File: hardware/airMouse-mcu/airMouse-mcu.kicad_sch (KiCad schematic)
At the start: 51 parts, among them J4 AT, J5 RADIO_PRG, J6 MCU_PRG, Q1 IRLML6346, SW60 KEY, U1 STM32G071RBTx, U2 AP1603, U3 ESP32-C3-WROOM-02U, U4 LSM6DS3

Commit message: add mouse pcb
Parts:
- J1: renamed from J6; Field5 (none) -> S5B-ZR-SM4A-TF (LF)(SN)
- J2: renamed from J5; Field5 (none) -> S3B-ZR-SM4A-TF (LF)(SN)
- J3: renamed from J4; Field5 (none) -> S3B-ZR-SM4A-TF (LF)(SN)
- R6: renamed from R62; footprint (none) -> Resistor_SMD:R_0603_1608Metric
- renumbered C26 to C10, C27 to C11, C35 to C12, C30 to C13, C31 to C14, C32 to C15, C3 to C2, C34 to C3, C2 to C4, C33 to C5, C5 to C6, C4 to C7, C29 to C8, C28 to C9, D13 to D2, D43 to D3, D12 to D4, R58 to R1, R52 to R10, R53 to R11, R47 to R12, R48 to R13, R46 to R14, R56 to R15, R54 to R16, R57 to R17, R59 to R2, R61 to R3, R60 to R4, R49 to R5, R50 to R7, R51 to R8, R55 to R9, SW60 to SW1, U4 to U1, U1 to U3, U3 to U4
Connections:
- net BAT+: no longer C12.1
- net ADC: now reaches R6.1, U3.27 (PB0)
- net ADC: now also C12.1
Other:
- note added: "additional parts: 1x ZH plug ZHR-3 1x ZH plug ZHR-5 8x ZH pin w/ cable SZH-200BK26 1x FPC 4p 10-04-A-0050-C-4-08-4-T 1x FPC 10p 10-10-A-0050-C-4-08-4-T 1x FPC 16p 10-16-A-0050-C-4-08-4-T"
- note removed: "additional parts: 1x ZH plug ZHR-3 1x ZH plug ZHR-5 8x ZH pin w/ cable SZH-200BK26 1x FPC 10p 10-10-A-0050-C-4-08-4-T 1x FPC 16p 10-16-A-0050-C-4-08-4-T"
- moved on the sheet: C12, J1, J2, J3, R11, R15, R6, R7, R9

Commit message: thumb pcb
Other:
- note removed: "DS1020-07-10VBT1A-R"
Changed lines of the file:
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@@
-		)
-	)
-	(text "DS1020-07-10VBT1A-R"
-		(exclude_from_sim no)
-		(at 77.47 128.27 0)
-		(effects
-			(font
-				(size 1.27 1.27)
-			)
 		)
 	)

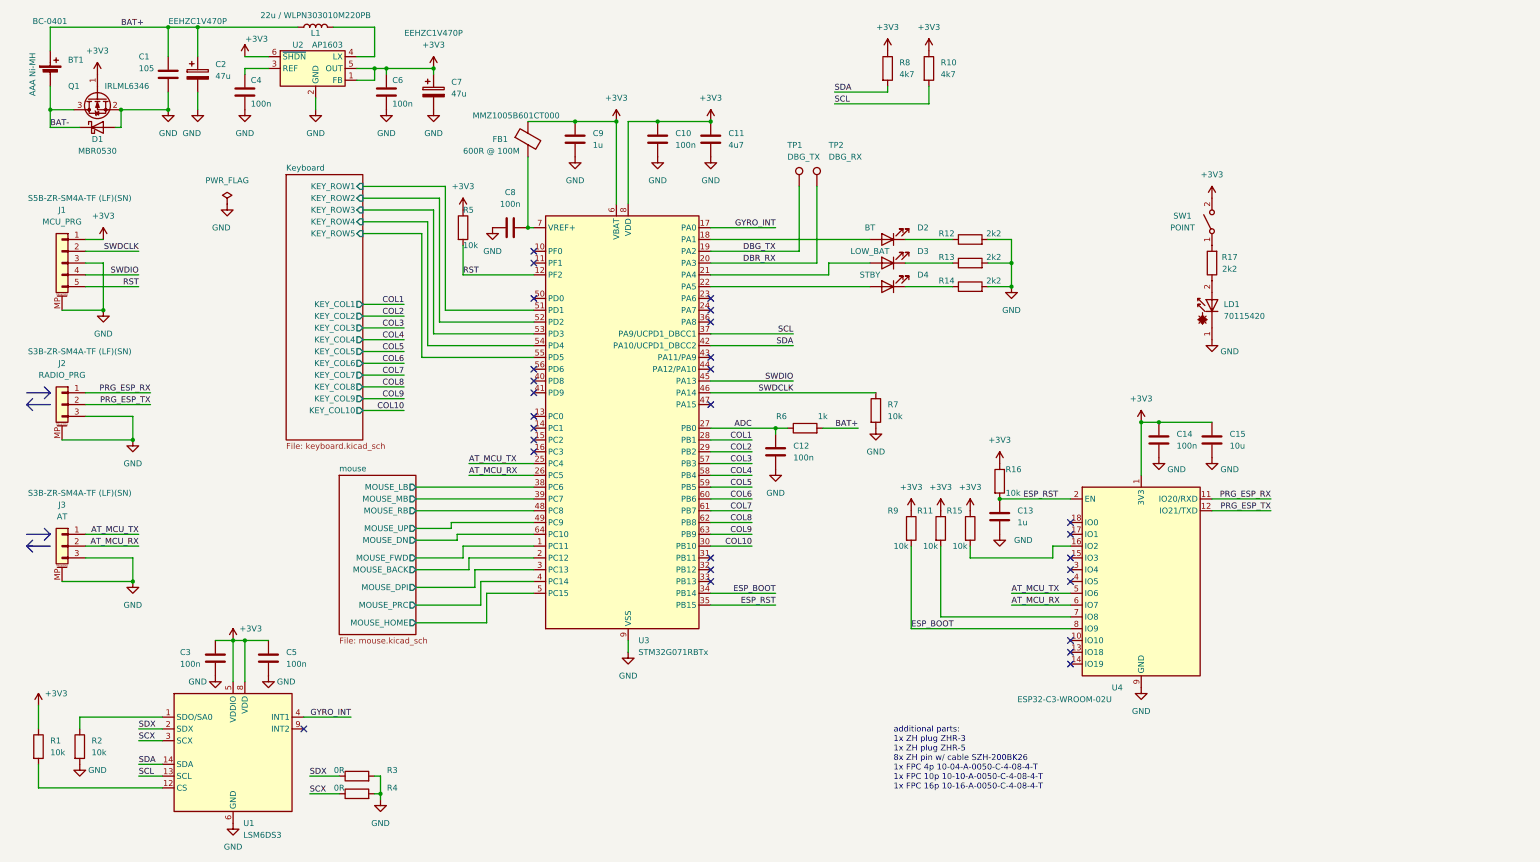
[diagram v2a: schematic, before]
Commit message: components placed on mcu board
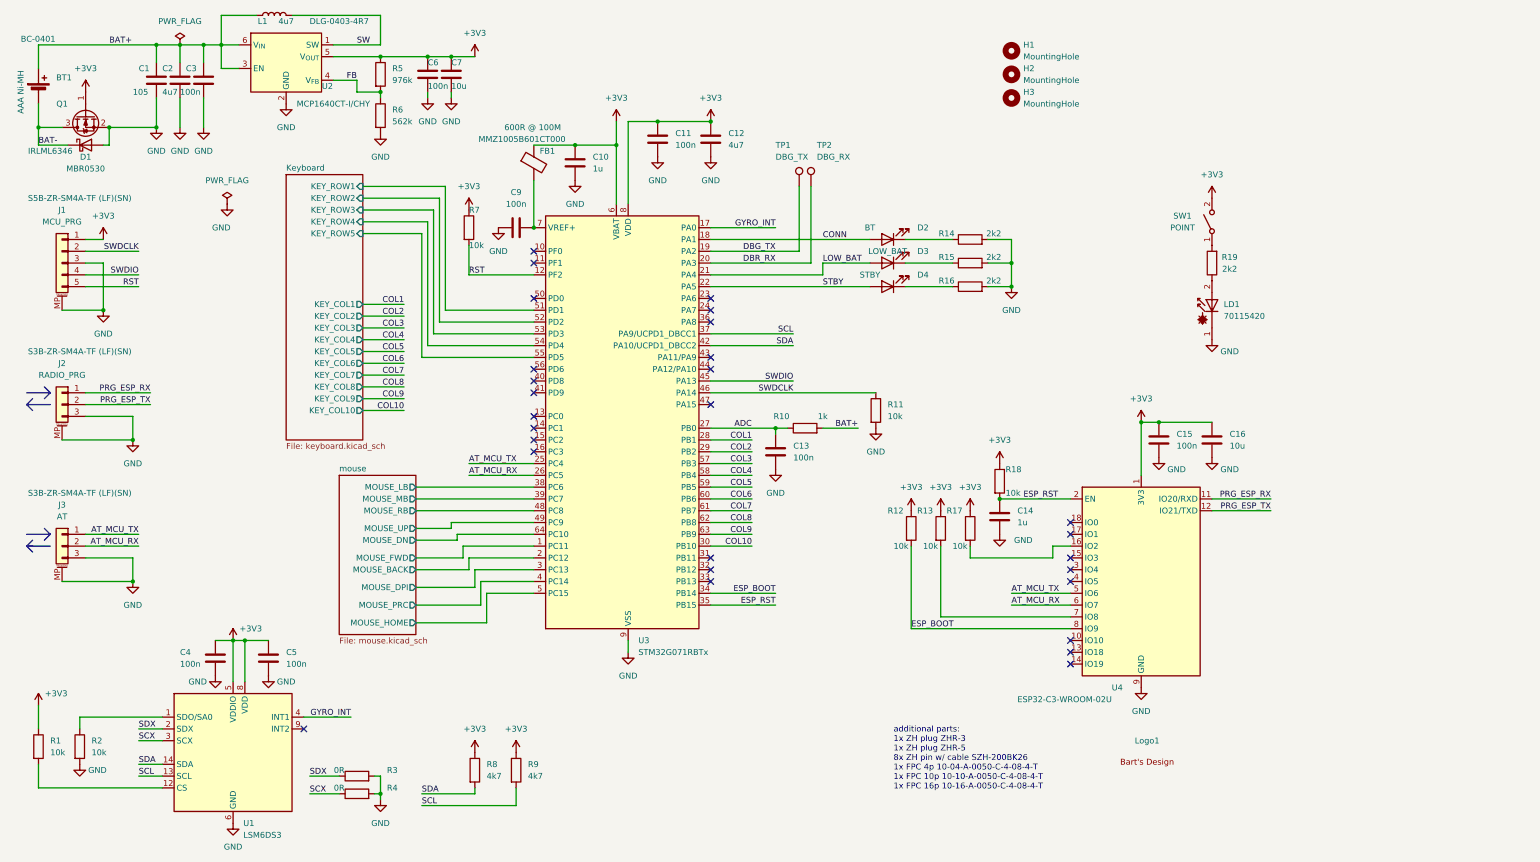
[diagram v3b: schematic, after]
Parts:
- removed C2, C7: 47u, Capacitor_SMD:CP_Elec_6.3x5.8, symbol Device:C_Polarized
- removed C4: 100n, Capacitor_SMD:C_0603_1608Metric, symbol Device:C
- removed U2: AP1603, Package_TO_SOT_SMD:SOT-23-6, symbol airMouseLib:AP1603
- added C2: 4u7, Capacitor_SMD:C_0805_2012Metric, symbol Device:C
- added C3: 100n, Capacitor_SMD:C_0603_1608Metric, symbol Device:C
- added C7: 10u, Capacitor_SMD:C_1206_3216Metric, symbol Device:C
- added H1, H2, H3: MountingHole, MountingHole:MountingHole_2.2mm_M2_ISO14580, symbol Mechanical:MountingHole
- added Logo1: ~, airMouseLib:Bart's Design 30mm, symbol airMouseLib:Bart's_Design_logo
- added R5: 976k, Resistor_SMD:R_0603_1608Metric, symbol Device:R
- added R6: 562k, Resistor_SMD:R_0603_1608Metric, symbol Device:R
- added U2: MCP1640CT-I/CHY, Package_TO_SOT_SMD:SOT-23-6, symbol Regulator_Switching:MCP1640Cx-xCHY
- L1: value 22u / WLPN303010M220PB -> 4u7; footprint Inductor_SMD:L_Abracon_ASPI-3012S -> Inductor_SMD:L_Ferrocore_DLG-0403; Field5 (none) -> DLG-0403-4R7
- renumbered C9 to C10, C10 to C11, C11 to C12, C12 to C13, C13 to C14, C14 to C15, C15 to C16, C3 to C4, C8 to C9, R6 to R10, R7 to R11, R9 to R12, R11 to R13, R12 to R14, R13 to R15, R14 to R16, R15 to R17, R16 to R18, R17 to R19, R5 to R7, R10 to R9
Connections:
- net +3V3: now also C7.1, R5.1, U2.5 (V_{OUT})
- net BAT+: now also C2.1, C3.1, U2.3 (EN), U2.6 (V_{IN})
- net GND: now also C2.2, C3.2, C7.2, R6.2, U2.2 (GND)
- net SW: now reaches L1.2
- net SW: now also U2.1 (SW)
- net LOW_BAT: now reaches D3.2 (A), U3.21 (PA4)
- net CONN: now reaches D2.2 (A), U3.18 (PA1)
- net STBY: now reaches D4.2 (A), U3.22 (PA5)
- new net FB: R5.2, R6.1, U2.4 (V_{FB})
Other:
- moved on the sheet: BT1, C1, C10, C9, D1, FB1, Q1, R7, R8, R9, TP2

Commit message: add mcu board
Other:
- title: EtherPointer -> EtherPointer mcu
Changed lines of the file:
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@@
 	(paper "A4")
 	(title_block
-		(title "EtherPointer")
-		(date "2025-02-13")
+		(title "EtherPointer mcu")
+		(date "2025-02-15")
 		(rev "RC1")
 		(company "Bart's Design")

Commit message: initializing housing
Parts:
- C1: value 105 -> 1u
- U1: value LSM6DS3 -> LSM6DS3TR-C
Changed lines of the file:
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@@
 			)
 		)
-		(property "Value" "105"
+		(property "Value" "1u"
 			(at 38.1 30.48 0)
 			(effects
@@
 			)
 		)
-		(property "Value" "LSM6DS3"
+		(property "Value" "LSM6DS3TR-C"
 			(at 61.8841 190.5 0)
 			(effects

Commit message: add connectors 3d models
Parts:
- J1: footprint Connector_JST:JST_ZH_S5B-ZR-SM4A-TF_1x05-1MP_P1.50mm_Horizontal -> airMouseLib:JST_ZH_S5B-ZR-SM4A-TF_1x05-1MP_P1.50mm_Horizontal
- J2, J3: footprint Connector_JST:JST_ZH_S3B-ZR-SM4A-TF_1x03-1MP_P1.50mm_Horizontal -> airMouseLib:JST_ZH_S3B-ZR-SM4A-TF_1x03-1MP_P1.50mm_Horizontal
- L1: footprint Inductor_SMD:L_Ferrocore_DLG-0403 -> airMouseLib:L_Ferrocore_DLG-0403
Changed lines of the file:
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@@
 (kicad_sch
-	(version 20231120)
+	(version 20250114)
 	(generator "eeschema")
-	(generator_version "8.0")
+	(generator_version "9.0")
 	(paper "A4")
 	(title_block
@@
 		(comment 1 "Bartosz Pracz")
 	)
+	(text "additional parts:\n1x ZH plug ZHR-3\n1x ZH plug ZHR-5\n8x ZH pin w/ cable SZH-200BK26\n1x FPC 4p 10-04-A-0050-C-4-08-4-T\n1x FPC 10p 10-10-A-0050-C-4-08-4-T\n1x FPC 16p 10-16-A-0050-C-4-08-4-T"
+		(exclude_from_sim no)
+		(at 201.93 173.99 0)
+		(effects
+			(font
+				(size 1.27 1.27)
+			)
+			(justify left)
+		)
+	)
 	(junction
 		(at 62.23 148.59)
@@
 		)
 	)
-	(text "additional parts:\n1x ZH plug ZHR-3\n1x ZH plug ZHR-5\n8x ZH pin w/ cable SZH-200BK26\n1x FPC 4p 10-04-A-0050-C-4-08-4-T\n1x FPC 10p 10-10-A-0050-C-4-08-4-T\n1x FPC 16p 10-16-A-0050-C-4-08-4-T"
-		(exclude_from_sim no)
-		(at 201.93 173.99 0)
-		(effects
-			(font
-				(size 1.27 1.27)
-			)
-			(justify left)
-		)
-	)
 	(label "SDA"
 		(at 100.33 181.61 0)
-		(fields_autoplaced yes)
 		(effects
 			(font
@@
 	(label "COL7"
 		(at 171.45 120.65 180)
-		(fields_autoplaced yes)
 		(effects
 			(font
@@
 	(label "COL4"
 		(at 171.45 113.03 180)
-		(fields_autoplaced yes)
 		(effects
 			(font
@@
 	(label "COL4"
 		(at 96.52 83.82 180)
-		(fields_autoplaced yes)
 		(effects
 			(font
@@
 	(label "AT_MCU_RX"
 		(at 110.49 113.03 0)
-		(fields_autoplaced yes)
 		(effects
 			(font
@@
 	(label "COL5"
 		(at 171.45 115.57 180)
-		(fields_autoplaced yes)
 		(effects
 			(font
@@
 	(label "BAT-"
 		(at 17.78 41.91 0)
-		(fields_autoplaced yes)
 		(effects
 			(font
@@
 	(label "COL2"
 		(at 96.52 78.74 180)
-		(fields_autoplaced yes)
 		(effects
 			(font
@@
 	(label "PRG_ESP_RX"
 		(at 41.91 95.25 180)
-		(fields_autoplaced yes)
 		(effects
 			(font
@@
 	(label "COL10"
 		(at 171.45 128.27 180)
-		(fields_autoplaced yes)
 		(effects
 			(font
@@
 	(label "COL6"
 		(at 96.52 88.9 180)
-		(fields_autoplaced yes)
 		(effects
 			(font
@@
 	(label "DBR_RX"
 		(at 176.53 67.31 180)
-		(fields_autoplaced yes)
 		(effects
 			(font
@@
 	(label "RST"
 		(at 39.37 72.39 180)
-		(fields_autoplaced yes)
 		(effects
 			(font
@@
 	(label "COL5"
 		(at 96.52 86.36 180)
-		(fields_autoplaced yes)
 		(effects
 			(font
@@
 	(label "COL1"
 		(at 96.52 76.2 180)
-		(fields_autoplaced yes)
 		(effects
 			(font
@@
 	(label "AT_MCU_TX"
 		(at 227.33 138.43 0)
-		(fields_autoplaced yes)
 		(effects
 			(font
@@
 	(label "SWDCLK"
 		(at 39.37 64.77 180)
-		(fields_autoplaced yes)
 		(effects
 			(font
@@
 	(label "COL10"
 		(at 96.52 99.06 180)
-		(fields_autoplaced yes)
 		(effects
 			(font
@@
 	(label "COL1"
 		(at 171.45 105.41 180)
-		(fields_autoplaced yes)
 		(effects
 			(font
@@
 	(label "ESP_BOOT"
 		(at 176.53 138.43 180)
-		(fields_autoplaced yes)
 		(effects
 			(font
@@
 	(label "COL9"
 		(at 171.45 125.73 180)
-		(fields_autoplaced yes)
 		(effects
 			(font
@@
 	(label "BAT+"
 		(at 194.31 102.87 180)
-		(fields_autoplaced yes)
 		(effects
 			(font
@@
 	(label "AT_MCU_TX"
 		(at 39.37 125.73 180)
-		(fields_autoplaced yes)
 		(effects
 			(font
@@
 	(label "SCL"
 		(at 100.33 184.15 0)
-		(fields_autoplaced yes)
 		(effects
 			(font
@@
 	(label "GYRO_INT"
 		(at 176.53 59.69 180)
-		(fields_autoplaced yes)
 		(effects
 			(font
@@
 	(label "SCX"
 		(at 76.2 181.61 0)
-		(fields_autoplaced yes)
 		(effects
 			(font
@@
 	(label "COL7"
 		(at 96.52 91.44 180)
-		(fields_autoplaced yes)
 		(effects
 			(font
@@
 	(label "DBG_TX"
 		(at 176.53 64.77 180)
-		(fields_autoplaced yes)
 		(effects
 			(font
@@
 	(label "LOW_BAT"
 		(at 186.69 67.31 0)
-		(fields_autoplaced yes)
 		(effects
 			(font
@@
 	(label "ESP_BOOT"
 		(at 205.74 146.05 0)
-		(fields_autoplaced yes)
 		(effects
 			(font
@@
 	(label "SWDIO"
 		(at 39.37 69.85 180)
-		(fields_autoplaced yes)
 		(effects
 			(font
@@
 	(label "COL8"
 		(at 171.45 123.19 180)
-		(fields_autoplaced yes)
 		(effects
 			(font
@@
 	(label "ESP_RST"
 		(at 176.53 140.97 180)
-		(fields_autoplaced yes)
 		(effects
 			(font
@@
 	(label "COL3"
 		(at 171.45 110.49 180)
-		(fields_autoplaced yes)
 		(effects
 			(font
@@
 	(label "SDX"
 		(at 76.2 177.8 0)
-		(fields_autoplaced yes)
 		(effects
 			(font
@@
 	(label "RST"
 		(at 110.49 69.85 0)
-		(fields_autoplaced yes)
 		(effects
 			(font
@@
 	(label "SCL"
 		(at 180.34 82.55 180)
-		(fields_autoplaced yes)
 		(effects
 			(font
@@
 	(label "ADC"
 		(at 167.64 102.87 0)
-		(fields_autoplaced yes)
 		(effects
 			(font
@@
 	(label "COL8"
 		(at 96.52 93.98 180)
-		(fields_autoplaced yes)
 		(effects
 			(font
@@
 	(label "FB"
 		(at 86.36 27.94 180)
-		(fields_autoplaced yes)
 		(effects
 			(font
@@
 	(label "SWDIO"
 		(at 180.34 92.71 180)
-		(fields_autoplaced yes)
 		(effects
 			(font
@@
 	(label "SCL"
 		(at 39.37 177.8 0)
-		(fields_autoplaced yes)
 		(effects
 			(font
@@
 	(label "COL3"
 		(at 96.52 81.28 180)
-		(fields_autoplaced yes)
 		(effects
 			(font
@@
 	(label "BAT+"
 		(at 33.02 20.32 0)
-		(fields_autoplaced yes)
 		(effects
 			(font
@@
 	(label "COL6"
 		(at 171.45 118.11 180)
-		(fields_autoplaced yes)
 		(effects
 			(font
@@
 	(label "SDA"
 		(at 180.34 85.09 180)
-		(fields_autoplaced yes)
 		(effects
 			(font
@@
 	(label "COL9"
 		(at 96.52 96.52 180)
-		(fields_autoplaced yes)
 		(effects
 			(font
@@
 	(label "AT_MCU_RX"
 		(at 39.37 128.27 180)
-		(fields_autoplaced yes)
 		(effects
 			(font
@@
 	(label "STBY"
 		(at 186.69 72.39 0)
-		(fields_autoplaced yes)
 		(effects
 			(font
@@
 	(label "AT_MCU_TX"
 		(at 110.49 110.49 0)
-		(fields_autoplaced yes)
 		(effects
 			(font
@@
 	(label "AT_MCU_RX"
 		(at 227.33 140.97 0)
-		(fields_autoplaced yes)
 		(effects
 			(font
@@
 	(label "SW"
 		(at 86.36 20.32 0)
-		(fields_autoplaced yes)
 		(effects
 			(font
@@
 	(label "PRG_ESP_RX"
 		(at 283.21 118.11 180)
-		(fields_autoplaced yes)
 		(effects
 			(font
@@
 	(label "ESP_RST"
 		(at 229.87 118.11 0)
-		(fields_autoplaced yes)
 		(effects
 			(font
@@
 	(label "SDA"
 		(at 39.37 175.26 0)
-		(fields_autoplaced yes)
 		(effects
 			(font
@@
 	(label "COL2"
 		(at 171.45 107.95 180)
-		(fields_autoplaced yes)
 		(effects
 			(font
@@
 	(label "PRG_ESP_TX"
 		(at 283.21 120.65 180)
-		(fields_autoplaced yes)
 		(effects
 			(font
@@
 	(label "CONN"
 		(at 186.69 62.23 0)
-		(fields_autoplaced yes)
 		(effects
 			(font
@@
 	(label "SDX"
 		(at 39.37 167.64 0)
-		(fields_autoplaced yes)
 		(effects
 			(font
@@
 	(label "SCX"
 		(at 39.37 170.18 0)
-		(fields_autoplaced yes)
 		(effects
 			(font
@@
 	(label "GYRO_INT"
 		(at 85.09 165.1 180)
-		(fields_autoplaced yes)
 		(effects
 			(font
@@
 	(label "SWDCLK"
 		(at 180.34 95.25 180)
-		(fields_autoplaced yes)
 		(effects
 			(font
@@
 	(label "PRG_ESP_TX"
 		(at 41.91 97.79 180)
-		(fields_autoplaced yes)
 		(effects
 			(font
@@
 			)
 		)
-		(property "Footprint" "Connector_JST:JST_ZH_S5B-ZR-SM4A-TF_1x05-1MP_P1.50mm_Horizontal"
+		(property "Footprint" "airMouseLib:JST_ZH_S5B-ZR-SM4A-TF_1x05-1MP_P1.50mm_Horizontal"
 			(at 22.86 67.31 0)
 			(effects
@@
 			)
 		)
-		(property "Footprint" "Connector_JST:JST_ZH_S3B-ZR-SM4A-TF_1x03-1MP_P1.50mm_Horizontal"
+		(property "Footprint" "airMouseLib:JST_ZH_S3B-ZR-SM4A-TF_1x03-1MP_P1.50mm_Horizontal"
 			(at 22.86 128.27 0)
 			(effects
@@
 			)
 		)
-		(property "Footprint" "Connector_JST:JST_ZH_S3B-ZR-SM4A-TF_1x03-1MP_P1.50mm_Horizontal"
+		(property "Footprint" "airMouseLib:JST_ZH_S3B-ZR-SM4A-TF_1x03-1MP_P1.50mm_Horizontal"
 			(at 22.86 97.79 0)
 			(effects
@@
 			)
 		)
-		(property "Footprint" "Inductor_SMD:L_Ferrocore_DLG-0403"
+		(property "Footprint" "airMouseLib:L_Ferrocore_DLG-0403"
 			(at 68.58 13.97 0)
 			(effects
@@
 		(at 82.55 113.03)
 		(size 16.51 34.29)
+		(exclude_from_sim no)
+		(in_bom yes)
+		(on_board yes)
+		(dnp no)
 		(fields_autoplaced yes)
 		(stroke
@@
 		(at 71.12 48.26)
 		(size 16.51 57.15)
+		(exclude_from_sim no)
+		(in_bom yes)
+		(on_board yes)
+		(dnp no)
 		(fields_autoplaced yes)
 		(stroke
@@
 		)
 	)
+	(embedded_fonts no)
 )

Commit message: pending housing
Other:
- note added: "additional parts: 1x ZH plug ZHR-3 1x ZH plug ZHR-5 8x ZH pin w/ cable SZH-200BK26 1x FPC 04p 10-04-A-0050-C-4-08-4-T / 10-04-A-0101-C-4-08-4-T 1x FPC 10p 10-10-A-0050-C-4-08-4-T / 10-10-A-0101-C-4-08-4-T 1x FPC 16p 10-16-A-0050-C-4-08-4-T / 10-16-A-0101-C-4-08-4-T"
- note removed: "additional parts: 1x ZH plug ZHR-3 1x ZH plug ZHR-5 8x ZH pin w/ cable SZH-200BK26 1x FPC 4p 10-04-A-0050-C-4-08-4-T 1x FPC 10p 10-10-A-0050-C-4-08-4-T 1x FPC 16p 10-16-A-0050-C-4-08-4-T"
- moved on the sheet: Logo1
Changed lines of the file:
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@@
 		(comment 1 "Bartosz Pracz")
 	)
-	(text "additional parts:\n1x ZH plug ZHR-3\n1x ZH plug ZHR-5\n8x ZH pin w/ cable SZH-200BK26\n1x FPC 4p 10-04-A-0050-C-4-08-4-T\n1x FPC 10p 10-10-A-0050-C-4-08-4-T\n1x FPC 16p 10-16-A-0050-C-4-08-4-T"
+	(text "additional parts:\n1x ZH plug ZHR-3\n1x ZH plug ZHR-5\n8x ZH pin w/ cable SZH-200BK26\n1x FPC 04p 10-04-A-0050-C-4-08-4-T / 10-04-A-0101-C-4-08-4-T\n1x FPC 10p 10-10-A-0050-C-4-08-4-T / 10-10-A-0101-C-4-08-4-T\n1x FPC 16p 10-16-A-0050-C-4-08-4-T / 10-16-A-0101-C-4-08-4-T"
 		(exclude_from_sim no)
-		(at 201.93 173.99 0)
+		(at 198.12 173.99 0)
 		(effects
 			(font
@@
 	(symbol
 		(lib_id "airMouseLib:Bart's_Design_logo")
-		(at 256.54 173.99 0)
+		(at 184.15 172.72 0)
 		(unit 1)
 		(exclude_from_sim no)
@@
 		(fields_autoplaced yes)
 		(property "Reference" "Logo1"
-			(at 256.54 170.18 0)
+			(at 184.15 168.91 0)
 			(effects
 				(font
@@
 		)
 		(property "Value" "~"
-			(at 256.54 171.45 0)
+			(at 184.15 170.18 0)
 			(effects
 				(font
@@
 		)
 		(property "Footprint" "airMouseLib:Bart's Design 30mm"
-			(at 256.54 173.99 0)
+			(at 184.15 172.72 0)
 			(effects
 				(font
@@
 		)
 		(property "Datasheet" ""
-			(at 256.54 173.99 0)
+			(at 184.15 172.72 0)
 			(effects
 				(font
@@
 		)
 		(property "Description" ""
-			(at 256.54 173.99 0)
+			(at 184.15 172.72 0)
 			(effects
 				(font

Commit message: add todo
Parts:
- R19: value 2k2 -> 0R
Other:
- note added: "usunąć led lasera usunąć R3/R4 C7- zmienić na 0805"
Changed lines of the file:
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@@
 		)
 	)
+	(text "usunąć led lasera\nusunąć R3/R4\nC7- zmienić na 0805"
+		(exclude_from_sim no)
+		(at 326.39 148.59 0)
+		(effects
+			(font
+				(size 1.27 1.27)
+			)
+		)
+	)
 	(junction
 		(at 62.23 148.59)
@@
 			)
 		)
-		(property "Value" "2k2"
+		(property "Value" "0R"
 			(at 274.32 68.58 0)
 			(effects
